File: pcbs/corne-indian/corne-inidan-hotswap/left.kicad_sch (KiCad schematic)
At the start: 88 parts, among them J1 Conn_01x03_Pin, J2 Conn_01x04_Pin, J3 PJ-3136-B, SW1 SW_Push, SW10 SW_Push, SW11 SW_Push, SW12 SW_Push, SW13 SW_Push, SW14 SW_Push, SW15 SW_Push, SW16 SW_Push, SW17 SW_Push, SW18 SW_Push, SW19 SW_Push, SW2 SW_Push, SW20 SW_Push, SW21 SW_Push, SW3 SW_Push, SW4 SW_Push, SW5 SW_Push, SW6 SW_Push, SW7 SW_Push, SW8 SW_Push, SW9 SW_Push, U1 AP2127K-3.3, U2 RP2040, U3 W25Q32JVSS, U4 AMS1117-3.3, Y1 12Mhz

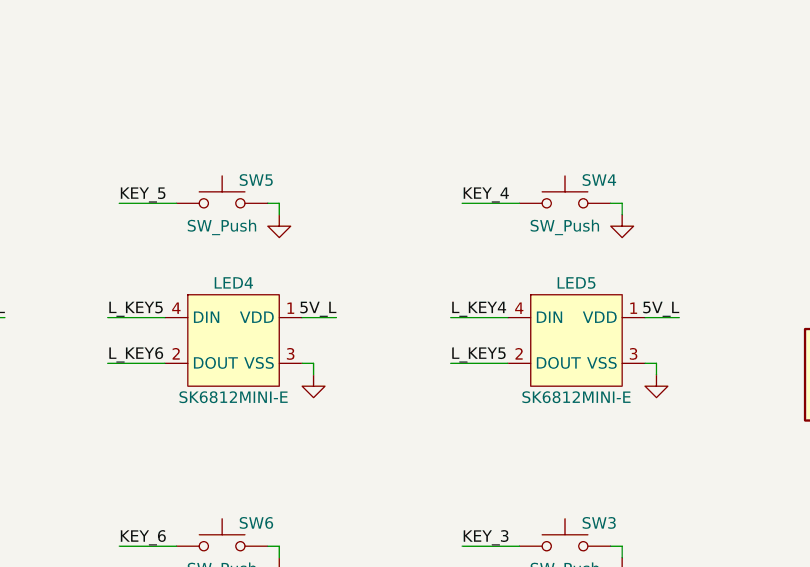
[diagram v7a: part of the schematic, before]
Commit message: Design almost done for routing some changes in the footprint
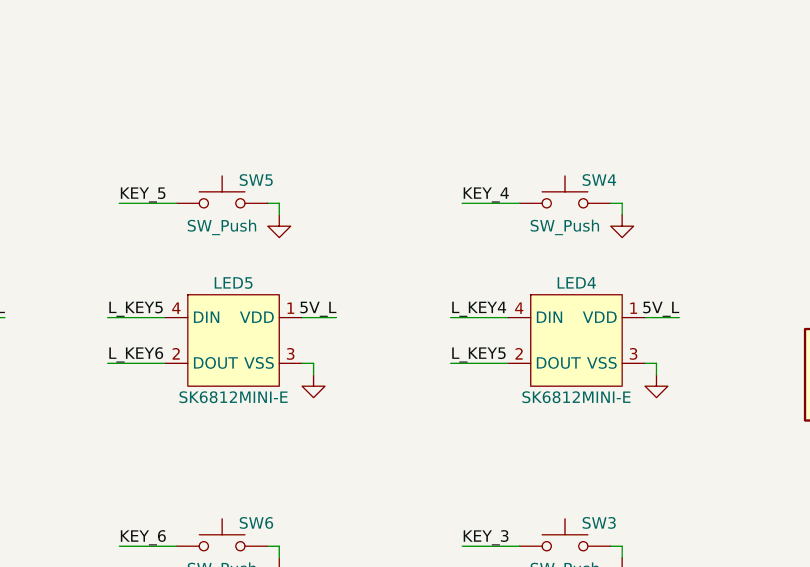
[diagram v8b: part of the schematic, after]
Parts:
- renumbered LED5 to LED4, LED4 to LED5
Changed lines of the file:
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@@
 		(on_board yes)
 		(dnp no)
-		(property "Reference" "LED5"
+		(property "Reference" "LED4"
 			(at 229.87 123.19 0)
 			(effects
@@
 			(project "corne-inidan-hotswap"
 				(path "/c90c0725-f1d3-4c5d-9757-c1f2f2a5449f/f4940f7d-bc6d-4495-a44d-e8b9a3eadf42"
-					(reference "LED5")
+					(reference "LED4")
 					(unit 1)
 				)
@@
 		(on_board yes)
 		(dnp no)
-		(property "Reference" "LED4"
+		(property "Reference" "LED5"
 			(at 191.77 123.19 0)
 			(effects
@@
 			(project "corne-inidan-hotswap"
 				(path "/c90c0725-f1d3-4c5d-9757-c1f2f2a5449f/f4940f7d-bc6d-4495-a44d-e8b9a3eadf42"
-					(reference "LED4")
+					(reference "LED5")
 					(unit 1)
 				)
